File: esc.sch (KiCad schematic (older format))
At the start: 78 parts, among them IC2 LM25101, IC3 LM25101, IC4 LM25101, IC5 ATMEGA8-AI, P1 CONN_01X03, P2 CONN_01X03, P3 CONN_01X02, P4 CONN_02X02, P5 CONN_01X01, P6 CONN_01X01, Q1 MOSFET_N, Q10 MOSFET_N, Q11 MOSFET_N, Q12 MOSFET_N, Q2 MOSFET_N, Q3 MOSFET_N, Q4 MOSFET_N, Q5 MOSFET_N, Q6 MOSFET_N, Q7 MOSFET_N, Q8 MOSFET_N, Q9 MOSFET_N, U1 MCP1804, U2 LM2940 10V, U3 LTV-356T, Y1 RESONATEUR

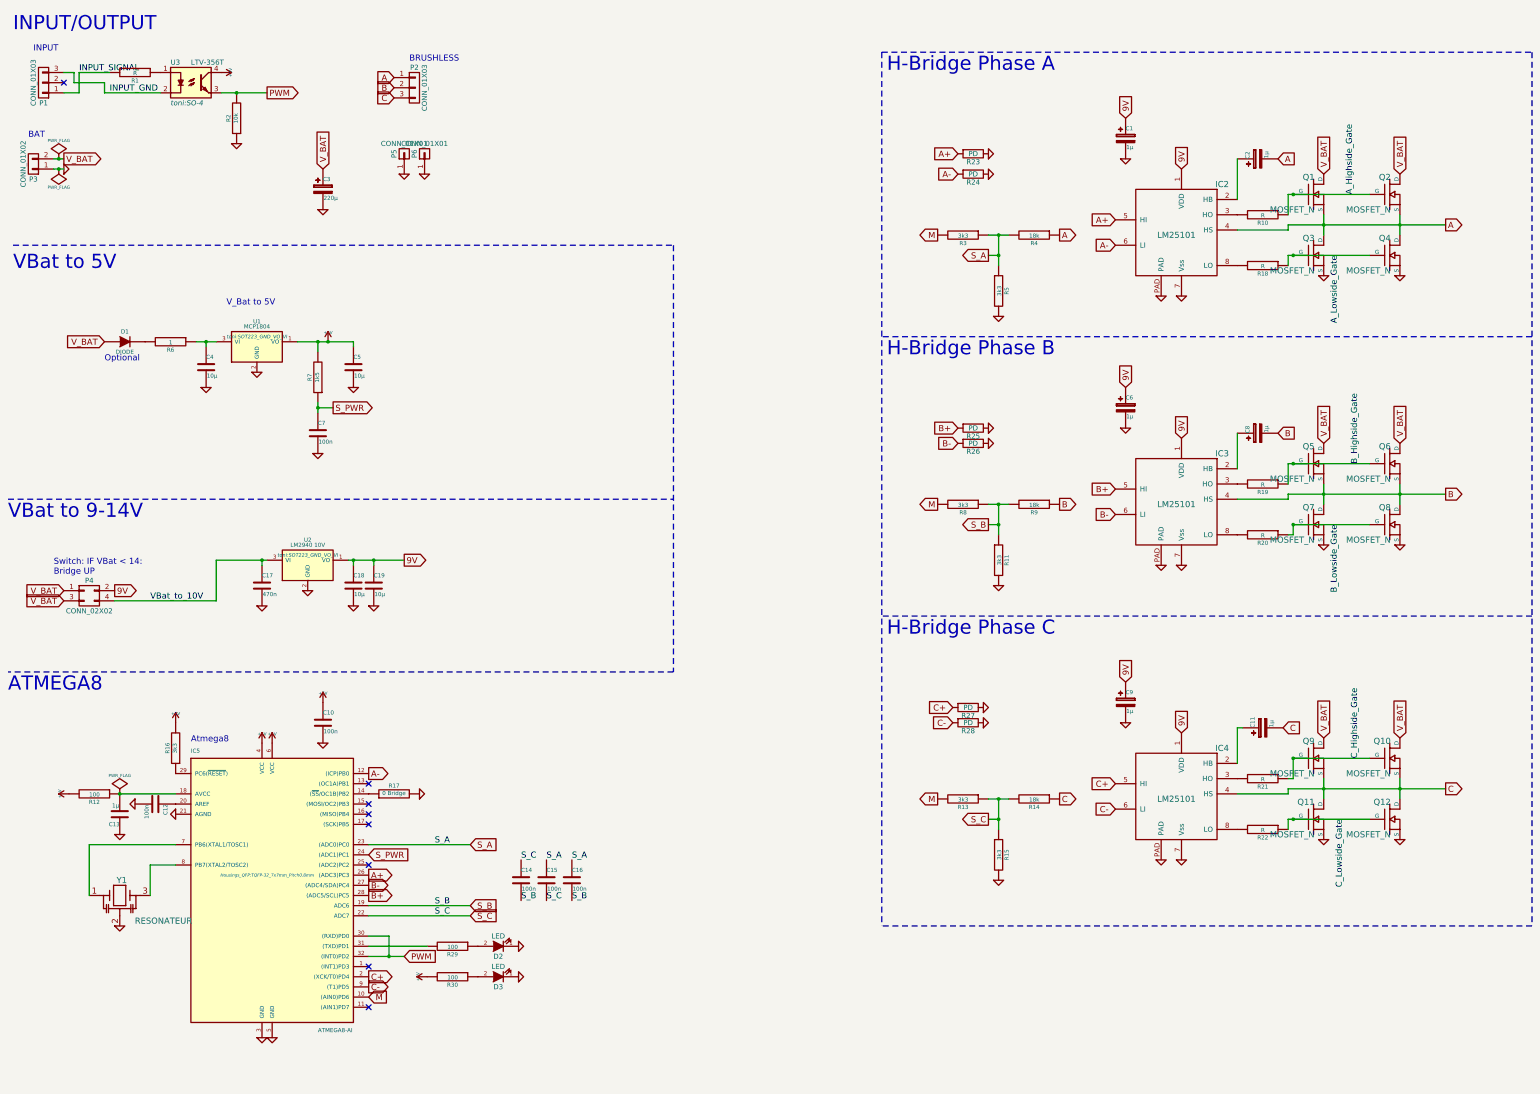
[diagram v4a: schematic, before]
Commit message: Getrennte Masse für Digital-Teil
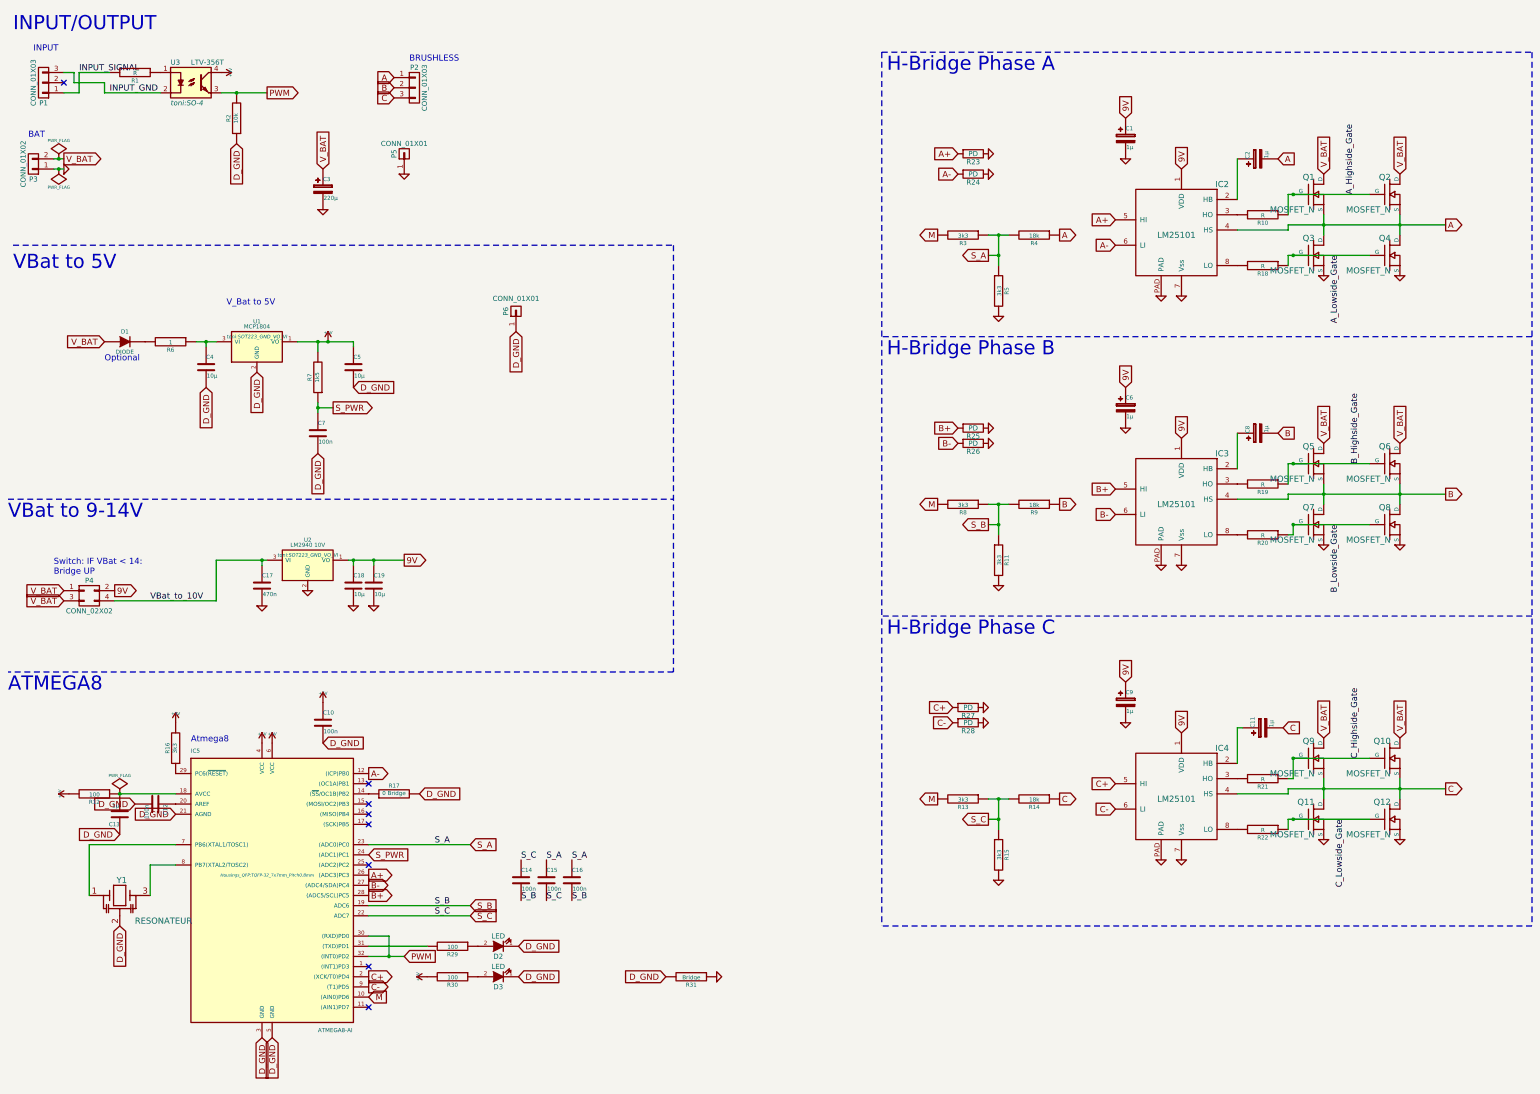
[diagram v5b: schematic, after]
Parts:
- added R31: Bridge, Resistors_SMD:R_1210_HandSoldering, symbol R-RESCUE-esc
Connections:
- net GND: now also R31.1; no longer C10.2, C12.2, C13.1, C4.2, C5.2, C7.2, D2.1 (K), D3.1 (K), IC5.21 (AGND), IC5.3 (GND), IC5.5 (GND), P6.1 (P1), R17.2, R2.1, U1.2 (GND), Y1.2
- new net D_GND: C10.2, C12.2, C13.1, C4.2, C5.2, C7.2, D2.1 (K), D3.1 (K), IC5.21 (AGND), IC5.3 (GND), IC5.5 (GND), P6.1 (P1), R17.2, R2.1, R31.2, U1.2 (GND), Y1.2
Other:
- moved on the sheet: P6

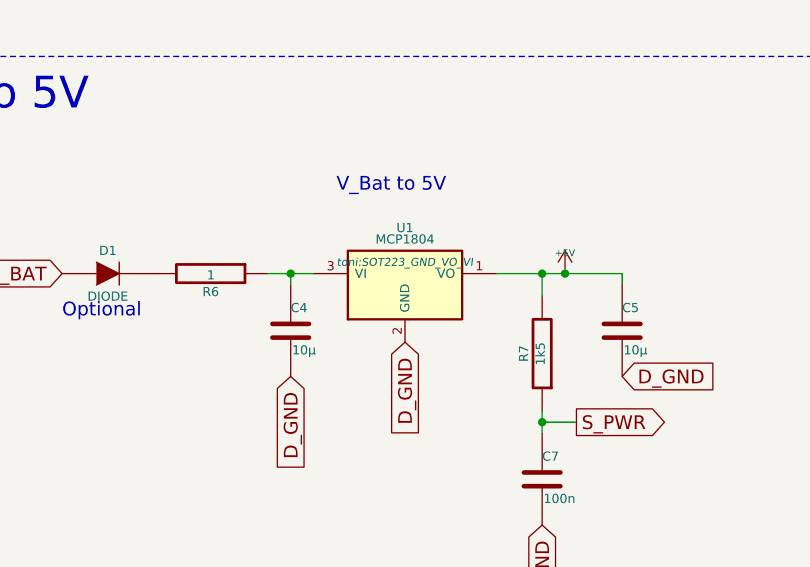
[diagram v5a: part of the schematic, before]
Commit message: Spannungswandler U1 geändert auf LD1117
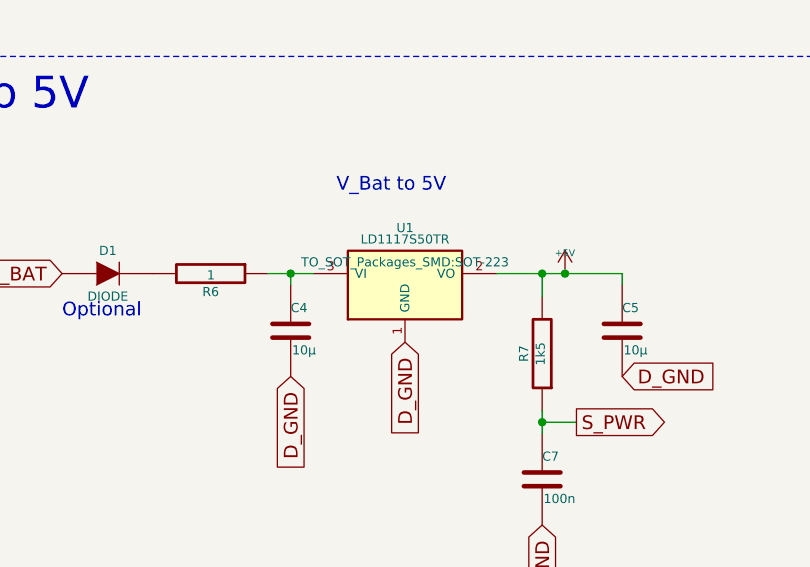
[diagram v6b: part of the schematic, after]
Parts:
- removed U1: MCP1804, toni:SOT223_GND_VO_VI, symbol LM2931AZ-5.0
- added U1: LD1117S50TR, TO_SOT_Packages_SMD:SOT-223, symbol LD1117S50TR
- Q1, Q10, Q11, Q12, Q2, Q3, Q4, Q5, Q6, Q7, Q8, Q9: footprint sven:SO8_WITH_Heatpipes -> Sven:SO8_WITH_Heatpipes_New
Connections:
- net +5V: now also U1.2 (VO)
- net D_GND: now also U1.1 (GND)
- net at C4.1, R6.1: now also U1.3 (VI)
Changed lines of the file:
@@
 Atmega8\n
-$Comp
-L LM2931AZ-5.0 U1
-U 1 1 564450C7
-P 3050 3800
-F 0 "U1" H 3050 4050 40  0000 C CNN
-F 1 "MCP1804" H 3050 4000 40  0000 C CNN
-F 2 "toni:SOT223_GND_VO_VI" H 3050 3900 35  0000 C CIN
-F 3 "" H 3050 3800 60  0000 C CNN
-	1    3050 3800
-	1    0    0    -1
-$EndComp
 $Comp
 L CONN_01X03 P2
@@
 F 0 "Q4" H 14210 3070 60  0000 R CNN
 F 1 "MOSFET_N" H 14210 2750 60  0000 R CNN
-F 2 "sven:SO8_WITH_Heatpipes" H 14200 2900 60  0001 C CNN
+F 2 "Sven:SO8_WITH_Heatpipes_New" H 14200 2900 60  0001 C CNN
 F 3 "" H 14200 2900 60  0000 C CNN
 	1    14200 2900
@@
 F 0 "Q3" H 13460 3070 60  0000 R CNN
 F 1 "MOSFET_N" H 13460 2750 60  0000 R CNN
-F 2 "sven:SO8_WITH_Heatpipes" H 13450 2900 60  0001 C CNN
+F 2 "Sven:SO8_WITH_Heatpipes_New" H 13450 2900 60  0001 C CNN
 F 3 "" H 13450 2900 60  0000 C CNN
 	1    13450 2900
@@
 F 0 "Q2" H 14210 2470 60  0000 R CNN
 F 1 "MOSFET_N" H 14210 2150 60  0000 R CNN
-F 2 "sven:SO8_WITH_Heatpipes" H 14200 2300 60  0001 C CNN
+F 2 "Sven:SO8_WITH_Heatpipes_New" H 14200 2300 60  0001 C CNN
 F 3 "" H 14200 2300 60  0000 C CNN
 	1    14200 2300
@@
 F 0 "Q1" H 13460 2470 60  0000 R CNN
 F 1 "MOSFET_N" H 13460 2150 60  0000 R CNN
-F 2 "sven:SO8_WITH_Heatpipes" H 13450 2300 60  0001 C CNN
+F 2 "Sven:SO8_WITH_Heatpipes_New" H 13450 2300 60  0001 C CNN
 F 3 "" H 13450 2300 60  0000 C CNN
 	1    13450 2300
@@
 F 0 "Q8" H 14210 5720 60  0000 R CNN
 F 1 "MOSFET_N" H 14210 5400 60  0000 R CNN
-F 2 "sven:SO8_WITH_Heatpipes" H 14200 5550 60  0001 C CNN
+F 2 "Sven:SO8_WITH_Heatpipes_New" H 14200 5550 60  0001 C CNN
 F 3 "" H 14200 5550 60  0000 C CNN
 	1    14200 5550
@@
 F 0 "Q7" H 13460 5720 60  0000 R CNN
 F 1 "MOSFET_N" H 13460 5400 60  0000 R CNN
-F 2 "sven:SO8_WITH_Heatpipes" H 13450 5550 60  0001 C CNN
+F 2 "Sven:SO8_WITH_Heatpipes_New" H 13450 5550 60  0001 C CNN
 F 3 "" H 13450 5550 60  0000 C CNN
 	1    13450 5550
@@
 F 0 "Q6" H 14210 5120 60  0000 R CNN
 F 1 "MOSFET_N" H 14210 4800 60  0000 R CNN
-F 2 "sven:SO8_WITH_Heatpipes" H 14200 4950 60  0001 C CNN
+F 2 "Sven:SO8_WITH_Heatpipes_New" H 14200 4950 60  0001 C CNN
 F 3 "" H 14200 4950 60  0000 C CNN
 	1    14200 4950
@@
 F 0 "Q5" H 13460 5120 60  0000 R CNN
 F 1 "MOSFET_N" H 13460 4800 60  0000 R CNN
-F 2 "sven:SO8_WITH_Heatpipes" H 13450 4950 60  0001 C CNN
+F 2 "Sven:SO8_WITH_Heatpipes_New" H 13450 4950 60  0001 C CNN
 F 3 "" H 13450 4950 60  0000 C CNN
 	1    13450 4950
@@
 F 0 "Q12" H 14210 8620 60  0000 R CNN
 F 1 "MOSFET_N" H 14210 8300 60  0000 R CNN
-F 2 "sven:SO8_WITH_Heatpipes" H 14200 8450 60  0001 C CNN
+F 2 "Sven:SO8_WITH_Heatpipes_New" H 14200 8450 60  0001 C CNN
 F 3 "" H 14200 8450 60  0000 C CNN
 	1    14200 8450
@@
 F 0 "Q11" H 13460 8620 60  0000 R CNN
 F 1 "MOSFET_N" H 13460 8300 60  0000 R CNN
-F 2 "sven:SO8_WITH_Heatpipes" H 13450 8450 60  0001 C CNN
+F 2 "Sven:SO8_WITH_Heatpipes_New" H 13450 8450 60  0001 C CNN
 F 3 "" H 13450 8450 60  0000 C CNN
 	1    13450 8450
@@
 F 0 "Q10" H 14210 8020 60  0000 R CNN
 F 1 "MOSFET_N" H 14210 7700 60  0000 R CNN
-F 2 "sven:SO8_WITH_Heatpipes" H 14200 7850 60  0001 C CNN
+F 2 "Sven:SO8_WITH_Heatpipes_New" H 14200 7850 60  0001 C CNN
 F 3 "" H 14200 7850 60  0000 C CNN
 	1    14200 7850
@@
 F 0 "Q9" H 13460 8020 60  0000 R CNN
 F 1 "MOSFET_N" H 13460 7700 60  0000 R CNN
-F 2 "sven:SO8_WITH_Heatpipes" H 13450 7850 60  0001 C CNN
+F 2 "Sven:SO8_WITH_Heatpipes_New" H 13450 7850 60  0001 C CNN
 F 3 "" H 13450 7850 60  0000 C CNN
 	1    13450 7850
@@
 Text GLabel 5600 3650 3    60   Input ~ 0
 D_GND
+$Comp
+L LD1117S50TR U1
+U 1 1 565C07C9
+P 3050 3800
+F 0 "U1" H 3050 4050 40  0000 C CNN
+F 1 "LD1117S50TR" H 3050 4000 40  0000 C CNN
+F 2 "TO_SOT_Packages_SMD:SOT-223" H 3050 3900 40  0000 C CNN
+F 3 "" H 3050 3800 60  0000 C CNN
+	1    3050 3800
+	1    0    0    -1
+$EndComp
 $EndSCHEMATC

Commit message: Versionierung geändert
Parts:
- C3: footprint Capacitors_Elko_ThroughHole:Elko_vert_11x5mm_RM2_CopperClear -> Capacitors_ThroughHole:C_Radial_D8_L13_P3.8
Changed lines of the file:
@@
 F 0 "C3" H 3700 2350 40  0000 L CNN
 F 1 "220µ" H 3706 2165 40  0000 L CNN
-F 2 "Capacitors_Elko_ThroughHole:Elko_vert_11x5mm_RM2_CopperClear" H 3738 2100 30  0001 C CNN
+F 2 "Capacitors_ThroughHole:C_Radial_D8_L13_P3.8" H 3738 2100 30  0001 C CNN
 F 3 "" H 3700 2250 60  0000 C CNN
 	1    3700 2250
